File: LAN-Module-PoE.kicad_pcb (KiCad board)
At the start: 2 copper layers, 25.3 x 61 mm, 105 parts, among them J1 HY931147C, J10 ProtoCastellatedHeader, J11 ProtoCastellatedHeader, J12 ProtoCastellatedHeader, J13 ProtoCastellatedHeader, J14 ProtoCastellatedHeader, J15 ProtoCastellatedHeader, J16 ProtoCastellatedHeader, J17 ProtoCastellatedHeader, J18 ProtoCastellatedHeader, J19 ProtoCastellatedHeader, J2 ProtoCastellatedHeader, J20 ProtoCastellatedHeader, J21 ProtoCastellatedHeader, J22 ProtoCastellatedHeader, J23 ProtoCastellatedHeader, J24 ProtoCastellatedHeader, J25 ProtoCastellatedHeader, J26 ProtoCastellatedHeader, J27 ProtoCastellatedHeader, J28 ProtoCastellatedHeader, J29 ProtoCastellatedHeader, J3 ProtoCastellatedHeader, J4 ProtoCastellatedHeader, J5 ProtoCastellatedHeader, J6 ProtoCastellatedHeader, J7 ProtoCastellatedHeader, J8 ProtoCastellatedHeader, J9 ProtoCastellatedHeader, SW1 RESET, U1 ESP32-U4WDH, U2 Si3404, U3 LV2842XLVDDCR, U4 RTL8201F, Y1 40MHz

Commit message: Update LCSC part numbers and adjust component values to available parts
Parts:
- C27: value 10u -> 22u
- R20: value 1.2R -> 0.62R
- R7: value 75R -> DNP
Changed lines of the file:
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@@
     (property "Sheetfile" "LAN-Module-PoE.kicad_sch")
     (property "Sheetname" "")
-    (property "Spec" "1%")
+    (property "Tolerance" "1%")
     (attr smd)
     (fp_text reference "R14" (at 0 -1.43) (layer "F.Fab")
@@
     (descr "SOT, 6 Pin (https://www.jedec.org/sites/default/files/docs/Mo-178c.PDF variant AB), generated with kicad-footprint-generator ipc_gullwing_generator.py")
     (tags "SOT TO_SOT_SMD")
+    (property "LCSC" "C225807")
     (property "Sheetfile" "LAN-Module-PoE.kicad_sch")
     (property "Sheetname" "")
@@
     (descr "Resistor SMD 0603 (1608 Metric), square (rectangular) end terminal, IPC_7351 nominal, (Body size source: IPC-SM-782 page 72, https://www.pcb-3d.com/wordpress/wp-content/uploads/ipc-sm-782a_amendment_1_and_2.pdf), generated with kicad-footprint-generator")
     (tags "resistor")
+    (property "LCSC" "C2930072")
     (property "Sheetfile" "LAN-Module-PoE.kicad_sch")
     (property "Sheetname" "")
@@
     (property "Sheetfile" "LAN-Module-PoE.kicad_sch")
     (property "Sheetname" "")
-    (property "Spec" "1%")
+    (property "Tolerance" "1%")
     (attr smd)
     (fp_text reference "R17" (at 0 -1.43) (layer "F.Fab")
@@
     (descr "Resistor SMD 0805 (2012 Metric), square (rectangular) end terminal, IPC_7351 nominal, (Body size source: IPC-SM-782 page 72, https://www.pcb-3d.com/wordpress/wp-content/uploads/ipc-sm-782a_amendment_1_and_2.pdf), generated with kicad-footprint-generator")
     (tags "resistor")
+    (property "LCSC" "C2930222")
     (property "Sheetfile" "LAN-Module-PoE.kicad_sch")
     (property "Sheetname" "")
@@
       (effects (font (size 1 1) (thickness 0.15)))
     )
-    (fp_text value "1.2R" (at 0 1.65 90) (layer "F.Fab")
+    (fp_text value "0.62R" (at 0 1.65 90) (layer "F.Fab")
       (effects (font (size 1 1) (thickness 0.15)))
     )
@@
     (descr "Inductor, Taiyo Yuden, NR series, Taiyo-Yuden_NR-40xx, 4.0mmx4.0mm")
     (tags "inductor taiyo-yuden nr smd")
+    (property "LCSC" "C222882")
+    (property "Part" "NRS4018T100MDGJ")
     (property "Sheetfile" "LAN-Module-PoE.kicad_sch")
     (property "Sheetname" "")
@@
     (tags "capacitor")
     (property "Dielectric" "X5R")
-    (property "Part1" "LCSC:C268016")
+    (property "LCSC" "C268016")
+    (property "Part" "UMK107BBJ225KA")
     (property "Range" "50V")
     (property "Sheetfile" "LAN-Module-PoE.kicad_sch")
@@
     (descr "QFN, 20 Pin (http://ww1.microchip.com/downloads/en/DeviceDoc/doc2535.pdf#page=164), generated with kicad-footprint-generator ipc_noLead_generator.py")
     (tags "QFN NoLead")
-    (property "Part" "LCSC:C461934")
+    (property "LCSC" "C461934")
     (property "Sheetfile" "LAN-Module-PoE.kicad_sch")
     (property "Sheetname" "")
@@
     (descr "Resistor SMD 0603 (1608 Metric), square (rectangular) end terminal, IPC_7351 nominal, (Body size source: IPC-SM-782 page 72, https://www.pcb-3d.com/wordpress/wp-content/uploads/ipc-sm-782a_amendment_1_and_2.pdf), generated with kicad-footprint-generator")
     (tags "resistor")
-    (property "Part" "LCSC:C2759402")
+    (property "LCSC" "C2759402")
     (property "Sheetfile" "LAN-Module-PoE.kicad_sch")
     (property "Sheetname" "")
-    (property "Spec" "1%")
+    (property "Tolerance" "1%")
     (attr smd)
     (fp_text reference "R13" (at 0 -1.43) (layer "F.Fab")
@@
     (descr "Resistor SMD 0603 (1608 Metric), square (rectangular) end terminal, IPC_7351 nominal, (Body size source: IPC-SM-782 page 72, https://www.pcb-3d.com/wordpress/wp-content/uploads/ipc-sm-782a_amendment_1_and_2.pdf), generated with kicad-footprint-generator")
     (tags "resistor")
+    (property "LCSC" "C2930079")
     (property "Sheetfile" "LAN-Module-PoE.kicad_sch")
     (property "Sheetname" "")
@@
     (descr "Inductor, Taiyo Yuden, NR series, Taiyo-Yuden_NR-80xx, 8.0mmx8.0mm")
     (tags "inductor taiyo-yuden nr smd")
+    (property "LCSC" "C2681905")
+    (property "Part" "YNR8065-330M")
+    (property "Rating" "1.2A")
     (property "Sheetfile" "LAN-Module-PoE.kicad_sch")
     (property "Sheetname" "")
@@
     (property "Sheetfile" "LAN-Module-PoE.kicad_sch")
     (property "Sheetname" "")
-    (property "Spec" "1%")
+    (property "Spec" "Tolerance")
     (attr smd)
     (fp_text reference "R18" (at 0 -1.43) (layer "F.Fab")
@@
     (descr "QFN, 32 Pin (http://ww1.microchip.com/downloads/en/DeviceDoc/8008S.pdf#page=20), generated with kicad-footprint-generator ipc_noLead_generator.py")
     (tags "QFN NoLead")
-    (property "Part1" "LCSC:C2763557")
-    (property "Part2" "LCSC:C45044")
+    (property "LCSC" "C2763557/C45044")
     (property "Sheetfile" "LAN-Module-PoE.kicad_sch")
     (property "Sheetname" "")
@@
     (tags "capacitor")
     (property "Dielectric" "X5R")
-    (property "Part1" "")
+    (property "LCSC" "C385977")
+    (property "Part" "HMK212BC7105KGHTE")
     (property "Range" "100V")
     (property "Sheetfile" "LAN-Module-PoE.kicad_sch")
@@
     (descr "Resistor SMD 0603 (1608 Metric), square (rectangular) end terminal, IPC_7351 nominal, (Body size source: IPC-SM-782 page 72, https://www.pcb-3d.com/wordpress/wp-content/uploads/ipc-sm-782a_amendment_1_and_2.pdf), generated with kicad-footprint-generator")
     (tags "resistor")
-    (property "MfrPart" "BLM18KG601SN1D ")
-    (property "Part1" "LCSC:C85833")
+    (property "LCSC" "C85833")
+    (property "Part" "BLM18KG601SN1D ")
     (property "Sheetfile" "LAN-Module-PoE.kicad_sch")
     (property "Sheetname" "")
@@
     (tags "capacitor")
     (property "Dielectric" "X5R")
-    (property "Part1" "")
     (property "Range" "100V")
     (property "Sheetfile" "LAN-Module-PoE.kicad_sch")
@@
     (descr "Capacitor SMD 0603 (1608 Metric), square (rectangular) end terminal, IPC_7351 nominal, (Body size source: IPC-SM-782 page 76, https://www.pcb-3d.com/wordpress/wp-content/uploads/ipc-sm-782a_amendment_1_and_2.pdf), generated with kicad-footprint-generator")
     (tags "capacitor")
-    (property "Part1" "")
+    (property "LCSC" "C113803")
+    (property "Part" "CC0603KRX7R0BB104")
     (property "Range" "100V")
     (property "Sheetfile" "LAN-Module-PoE.kicad_sch")
@@
     (tags "capacitor")
     (property "Dielectric" "X5R")
-    (property "Part1" "")
     (property "Range" "100V")
     (property "Sheetfile" "LAN-Module-PoE.kicad_sch")
@@
     (descr "SMD capacitor, aluminum electrolytic nonpolar, 6.3x5.4mm")
     (tags "capacitor electrolyic nonpolar")
+    (property "LCSC" "C487431")
+    (property "Part" "VKMC1002A220MV")
     (property "Range" "100V")
     (property "Sheetfile" "LAN-Module-PoE.kicad_sch")
@@
       (effects (font (size 1 1) (thickness 0.15)))
     )
-    (fp_text value "10u" (at 0 4.35) (layer "F.Fab")
+    (fp_text value "22u" (at 0 4.35) (layer "F.Fab")
       (effects (font (size 1 1) (thickness 0.15)))
     )
@@
     (descr "LAN-Transformer WE-RJ45LAN 10/100/1000 BaseT")
     (tags "ethernet lan connector")
-    (property "Part" "LCSC:C12074")
+    (property "LCSC" "C12074")
     (property "Sheetfile" "LAN-Module-PoE.kicad_sch")
     (property "Sheetname" "")
@@
     (descr "Resistor SMD 0603 (1608 Metric), square (rectangular) end terminal, IPC_7351 nominal, (Body size source: IPC-SM-782 page 72, https://www.pcb-3d.com/wordpress/wp-content/uploads/ipc-sm-782a_amendment_1_and_2.pdf), generated with kicad-footprint-generator")
     (tags "resistor")
-    (property "MfrPart" "BLM18KG601SN1D ")
-    (property "Part1" "LCSC:C85833")
+    (property "LCSC" "C85833")
+    (property "Part" "BLM18KG601SN1D ")
     (property "Sheetfile" "LAN-Module-PoE.kicad_sch")
     (property "Sheetname" "")
@@
     (tags "capacitor")
     (property "Dielectric" "X5R")
-    (property "Part1" "LCSC:C268016")
+    (property "LCSC" "C268016")
+    (property "Part" "UMK107BBJ225KA")
     (property "Range" "50V")
     (property "Sheetfile" "LAN-Module-PoE.kicad_sch")
@@
     (descr "QFN, 48 Pin (https://www.espressif.com/sites/default/files/documentation/esp32_datasheet_en.pdf#page=38), generated with kicad-footprint-generator ipc_noLead_generator.py")
     (tags "QFN NoLead")
-    (property "Part1" "LCSC:C529586")
-    (property "Part2" "LCSC:C967021")
+    (property "LCSC" "C529586/C3013932")
     (property "Sheetfile" "LAN-Module-PoE.kicad_sch")
     (property "Sheetname" "")
@@
       (effects (font (size 1 1) (thickness 0.15)))
     )
-    (fp_text value "75R" (at 0 1.43 90) (layer "F.Fab")
+    (fp_text value "DNP" (at 0 1.43 90) (layer "F.Fab")
       (effects (font (size 1 1) (thickness 0.15)))
     )
@@
     (descr "SMD Crystal SERIES SMD3225/4 http://www.txccrystal.com/images/pdf/7m-accuracy.pdf, 3.2x2.5mm^2 package")
     (tags "SMD SMT crystal")
-    (property "Part1" "LCSC:C9010")
-    (property "Part2" "LCSC:C555624")
+    (property "LCSC" "C9010/C555624")
     (property "Sheetfile" "LAN-Module-PoE.kicad_sch")
     (property "Sheetname" "")

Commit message: Rev2.1 changes
Just changing component attributes, no design changes
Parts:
- C14: value 4.7u -> 10u
- D2: value PMEG6020ER,115 -> B5819W
- R15, R16: value 240R -> 270R
- R21: value 47k -> 33k
- R22, R4: value 499R -> 510R
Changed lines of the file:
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@@
     (descr "SOD-123")
     (tags "SOD-123")
+    (property "LCSC" "C2685454")
+    (property "Rating" "1A 40V")
     (property "Sheetfile" "LAN-Module-PoE.kicad_sch")
     (property "Sheetname" "")
@@
       (effects (font (size 1 1) (thickness 0.15)))
     )
-    (fp_text value "PMEG6020ER,115" (at 0 2.1) (layer "F.Fab")
+    (fp_text value "B5819W" (at 0 2.1) (layer "F.Fab")
       (effects (font (size 1 1) (thickness 0.15)))
     )
@@
     (descr "Capacitor SMD 0805 (2012 Metric), square (rectangular) end terminal, IPC_7351 nominal, (Body size source: IPC-SM-782 page 76, https://www.pcb-3d.com/wordpress/wp-content/uploads/ipc-sm-782a_amendment_1_and_2.pdf, https://docs.google.com/spreadsheets/d/1BsfQQcO9C6DZCsRaXUlFlo91Tg2WpOkGARC1WS5S8t0/edit?usp=sharing), generated with kicad-footprint-generator")
     (tags "capacitor")
-    (property "Dielectric" "X5R")
     (property "LCSC" "C268016")
     (property "Part" "UMK107BBJ225KA")
@@
     (property "Sheetfile" "LAN-Module-PoE.kicad_sch")
     (property "Sheetname" "")
+    (property "Spec" "X5R")
     (attr smd)
     (fp_text reference "C29" (at 0 -1.68 90) (layer "F.SilkS") hide
@@
     (descr "Resistor SMD 0603 (1608 Metric), square (rectangular) end terminal, IPC_7351 nominal, (Body size source: IPC-SM-782 page 72, https://www.pcb-3d.com/wordpress/wp-content/uploads/ipc-sm-782a_amendment_1_and_2.pdf), generated with kicad-footprint-generator")
     (tags "resistor")
+    (property "LCSC" "C22548")
     (property "Sheetfile" "LAN-Module-PoE.kicad_sch")
     (property "Sheetname" "")
@@
     (descr "Resistor SMD 0603 (1608 Metric), square (rectangular) end terminal, IPC_7351 nominal, (Body size source: IPC-SM-782 page 72, https://www.pcb-3d.com/wordpress/wp-content/uploads/ipc-sm-782a_amendment_1_and_2.pdf), generated with kicad-footprint-generator")
     (tags "resistor")
+    (property "LCSC" "C126359 ")
     (property "Sheetfile" "LAN-Module-PoE.kicad_sch")
     (property "Sheetname" "")
@@
       (effects (font (size 1 1) (thickness 0.15)))
     )
-    (fp_text value "499R" (at 0 1.43) (layer "F.Fab")
+    (fp_text value "510R" (at 0 1.43) (layer "F.Fab")
       (effects (font (size 1 1) (thickness 0.15)))
     )
@@
     (descr "Capacitor SMD 0805 (2012 Metric), square (rectangular) end terminal, IPC_7351 nominal, (Body size source: IPC-SM-782 page 76, https://www.pcb-3d.com/wordpress/wp-content/uploads/ipc-sm-782a_amendment_1_and_2.pdf, https://docs.google.com/spreadsheets/d/1BsfQQcO9C6DZCsRaXUlFlo91Tg2WpOkGARC1WS5S8t0/edit?usp=sharing), generated with kicad-footprint-generator")
     (tags "capacitor")
-    (property "Dielectric" "X5R")
     (property "LCSC" "C385977")
     (property "Part" "HMK212BC7105KGHTE")
@@
     (property "Sheetfile" "LAN-Module-PoE.kicad_sch")
     (property "Sheetname" "")
+    (property "Spec" "X5R")
     (attr smd)
     (fp_text reference "C4" (at 0 -1.68 90) (layer "F.SilkS")
@@
     (descr "Capacitor SMD 0603 (1608 Metric), square (rectangular) end terminal, IPC_7351 nominal, (Body size source: IPC-SM-782 page 76, https://www.pcb-3d.com/wordpress/wp-content/uploads/ipc-sm-782a_amendment_1_and_2.pdf), generated with kicad-footprint-generator")
     (tags "capacitor")
-    (property "Dielectric" "X5R")
     (property "Range" "100V")
     (property "Sheetfile" "LAN-Module-PoE.kicad_sch")
     (property "Sheetname" "")
+    (property "Spec" "X5R")
     (property "exclude_from_bom" "")
     (attr smd exclude_from_bom)
@@
     (descr "Resistor SMD 0603 (1608 Metric), square (rectangular) end terminal, IPC_7351 nominal, (Body size source: IPC-SM-782 page 72, https://www.pcb-3d.com/wordpress/wp-content/uploads/ipc-sm-782a_amendment_1_and_2.pdf), generated with kicad-footprint-generator")
     (tags "resistor")
+    (property "LCSC" "C98220")
     (property "Sheetfile" "LAN-Module-PoE.kicad_sch")
     (property "Sheetname" "")
@@
       (effects (font (size 1 1) (thickness 0.15)))
     )
-    (fp_text value "47k" (at 0 1.43) (layer "F.Fab")
+    (fp_text value "33k" (at 0 1.43) (layer "F.Fab")
       (effects (font (size 1 1) (thickness 0.15)))
     )
@@
     (descr "Resistor SMD 0603 (1608 Metric), square (rectangular) end terminal, IPC_7351 nominal, (Body size source: IPC-SM-782 page 72, https://www.pcb-3d.com/wordpress/wp-content/uploads/ipc-sm-782a_amendment_1_and_2.pdf), generated with kicad-footprint-generator")
     (tags "resistor")
+    (property "LCSC" "C114637")
     (property "Sheetfile" "LAN-Module-PoE.kicad_sch")
     (property "Sheetname" "")
@@
     (descr "Capacitor SMD 0603 (1608 Metric), square (rectangular) end terminal, IPC_7351 nominal, (Body size source: IPC-SM-782 page 76, https://www.pcb-3d.com/wordpress/wp-content/uploads/ipc-sm-782a_amendment_1_and_2.pdf), generated with kicad-footprint-generator")
     (tags "capacitor")
-    (property "Dielectric" "X5R")
     (property "Range" "100V")
     (property "Sheetfile" "LAN-Module-PoE.kicad_sch")
     (property "Sheetname" "")
+    (property "Spec" "X5R")
     (property "exclude_from_bom" "")
     (attr smd exclude_from_bom)
@@
       (effects (font (size 1 1) (thickness 0.15)))
     )
-    (fp_text value "240R" (at 0 1.43 90) (layer "F.Fab")
+    (fp_text value "270R" (at 0 1.43 90) (layer "F.Fab")
       (effects (font (size 1 1) (thickness 0.15)))
     )
@@
       (effects (font (size 1 1) (thickness 0.15)))
     )
-    (fp_text value "499R" (at 0 1.43) (layer "F.Fab")
+    (fp_text value "510R" (at 0 1.43) (layer "F.Fab")
       (effects (font (size 1 1) (thickness 0.15)))
     )
@@
       (effects (font (size 1 1) (thickness 0.15)))
     )
-    (fp_text value "240R" (at 0 1.43 90) (layer "F.Fab")
+    (fp_text value "270R" (at 0 1.43 90) (layer "F.Fab")
       (effects (font (size 1 1) (thickness 0.15)))
     )
@@
       (effects (font (size 1 1) (thickness 0.15)))
     )
-    (fp_text value "4.7u" (at 0 1.43 90) (layer "F.Fab")
+    (fp_text value "10u" (at 0 1.43 90) (layer "F.Fab")
       (effects (font (size 1 1) (thickness 0.15)))
     )
@@
     (descr "Capacitor SMD 0805 (2012 Metric), square (rectangular) end terminal, IPC_7351 nominal, (Body size source: IPC-SM-782 page 76, https://www.pcb-3d.com/wordpress/wp-content/uploads/ipc-sm-782a_amendment_1_and_2.pdf, https://docs.google.com/spreadsheets/d/1BsfQQcO9C6DZCsRaXUlFlo91Tg2WpOkGARC1WS5S8t0/edit?usp=sharing), generated with kicad-footprint-generator")
     (tags "capacitor")
-    (property "Dielectric" "X5R")
     (property "LCSC" "C268016")
     (property "Part" "UMK107BBJ225KA")
@@
     (property "Sheetfile" "LAN-Module-PoE.kicad_sch")
     (property "Sheetname" "")
+    (property "Spec" "X5R")
     (attr smd)
     (fp_text reference "C18" (at 0 -1.68 90) (layer "F.Fab")

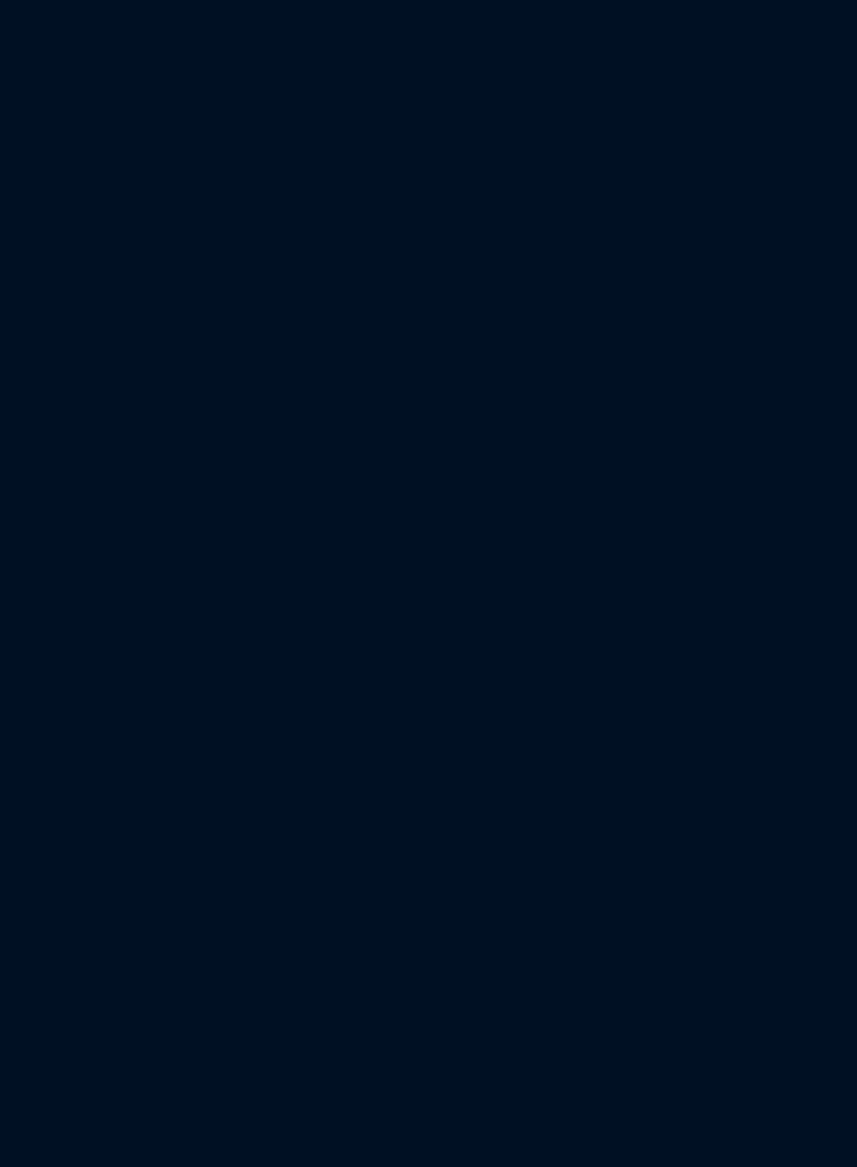
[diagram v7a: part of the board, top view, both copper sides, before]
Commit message: Update PoE PCB Kicad version
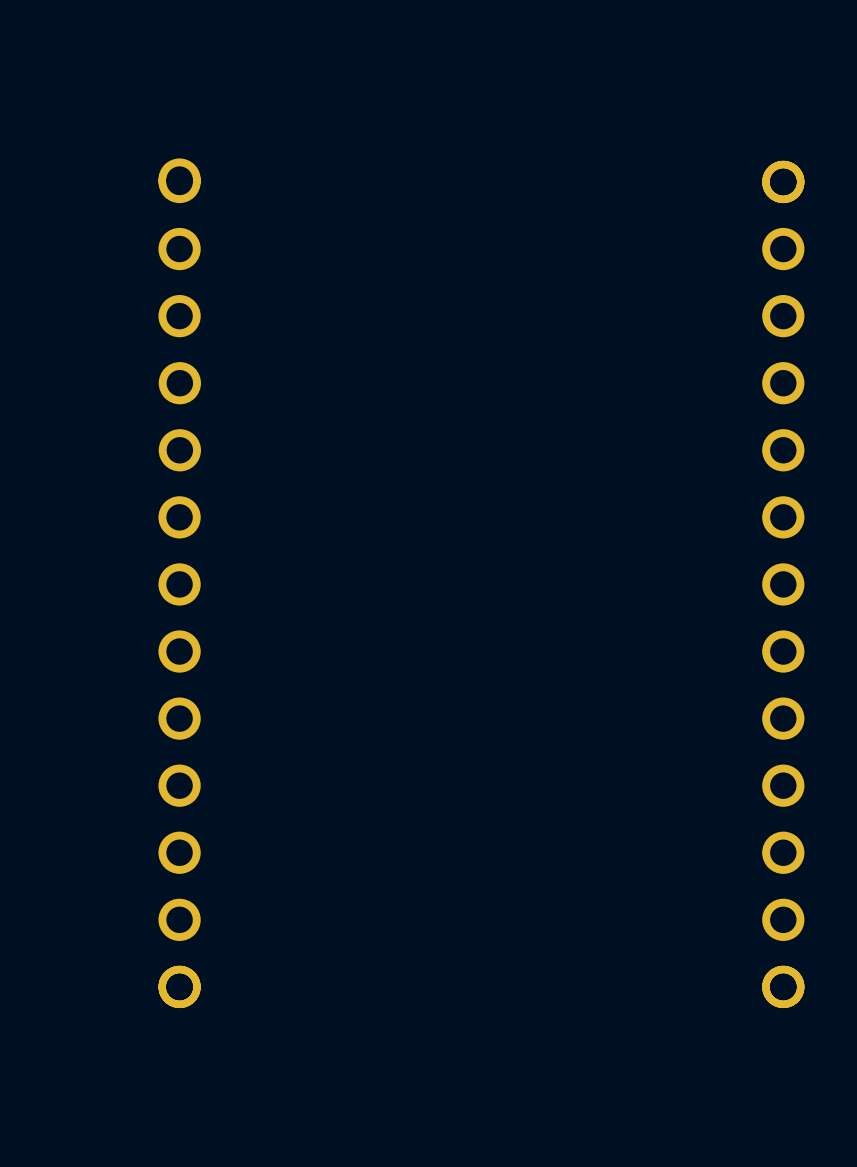
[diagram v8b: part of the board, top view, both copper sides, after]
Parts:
- added ?: , , F.Cu at (92.3, 39.4)
- added ?: , , F.Cu at (69.5, 39.3)
- added ?: , , F.Cu at (69.5, 69.8)
- added J10: ProtoCastellatedHeader, Visclib:ProtoHeader_65mil, F.Cu at (69.5, 57.1)
- added J11: ProtoCastellatedHeader, Visclib:ProtoHeader_65mil, F.Cu at (69.5, 59.7)
- added J12: ProtoCastellatedHeader, Visclib:ProtoHeader_65mil, F.Cu at (69.5, 62.2)
- added J13: ProtoCastellatedHeader, Visclib:ProtoHeader_65mil, F.Cu at (69.5, 64.8)
- added J14: ProtoCastellatedHeader, Visclib:ProtoHeader_65mil, F.Cu at (69.5, 67.3)
- added J15: ProtoCastellatedHeader, Visclib:ProtoHeader_65mil, F.Cu at (92.3, 64.8)
- added J16: ProtoCastellatedHeader, Visclib:ProtoHeader_65mil, F.Cu at (69.5, 69.8)
- added J17: ProtoCastellatedHeader, Visclib:ProtoHeader_65mil, F.Cu at (92.3, 39.4)
- added J18: ProtoCastellatedHeader, Visclib:ProtoHeader_65mil, F.Cu at (92.3, 41.9)
- added J19: ProtoCastellatedHeader, Visclib:ProtoHeader_65mil, F.Cu at (92.3, 44.5)
- added J20: ProtoCastellatedHeader, Visclib:ProtoHeader_65mil, F.Cu at (92.3, 47.0)
- added J21: ProtoCastellatedHeader, Visclib:ProtoHeader_65mil, F.Cu at (92.3, 49.5)
- added J22: ProtoCastellatedHeader, Visclib:ProtoHeader_65mil, F.Cu at (92.3, 52.1)
- added J23: ProtoCastellatedHeader, Visclib:ProtoHeader_65mil, F.Cu at (92.3, 54.6)
- added J24: ProtoCastellatedHeader, Visclib:ProtoHeader_65mil, F.Cu at (92.3, 57.1)
- added J25: ProtoCastellatedHeader, Visclib:ProtoHeader_65mil, F.Cu at (92.3, 59.7)
- added J26: ProtoCastellatedHeader, Visclib:ProtoHeader_65mil, F.Cu at (92.3, 62.2)
- added J27: ProtoCastellatedHeader, Visclib:ProtoHeader_65mil, F.Cu at (92.3, 67.3)
- added J28 (x2): ProtoCastellatedHeader, Visclib:ProtoHeader_65mil, F.Cu at (92.3, 69.8)
- added J3: ProtoCastellatedHeader, Visclib:ProtoHeader_65mil, F.Cu at (69.5, 39.4)
- added J4: ProtoCastellatedHeader, Visclib:ProtoHeader_65mil, F.Cu at (69.5, 41.9)
- added J5: ProtoCastellatedHeader, Visclib:ProtoHeader_65mil, F.Cu at (69.5, 44.5)
- added J6: ProtoCastellatedHeader, Visclib:ProtoHeader_65mil, F.Cu at (69.5, 47.0)
- added J7: ProtoCastellatedHeader, Visclib:ProtoHeader_65mil, F.Cu at (69.5, 49.5)
- added J8: ProtoCastellatedHeader, Visclib:ProtoHeader_65mil, F.Cu at (69.5, 52.1)
- added J9: ProtoCastellatedHeader, Visclib:ProtoHeader_65mil, F.Cu at (69.5, 54.6)
